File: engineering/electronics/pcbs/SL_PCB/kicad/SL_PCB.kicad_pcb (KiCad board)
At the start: 2 copper layers, 200 x 115 mm, 310 parts, among them J1 - Power +, J17 Temp, J19 Charger +, J32 Temp, J35 ET60S-D06-0-00-D06-X-V1-S, J37 DEBUG, J38 USB, Q1 IRFL4105PBF, Q11 DMG2305UX-7, Q12 DMG2305UX-7, Q13 DMG2305UX-7, Q14 DMG2305UX-7, Q15 DMG2305UX-7, Q16 DMG2305UX-7, Q17 DMG2305UX-7, Q18 DMG2305UX-7, Q19 DMG2305UX-7, Q20 DMG2305UX-7, Q21 DMG2305UX-7, Q22 DMG2305UX-7, Q23 DMG2305UX-7, Q24 DMG2305UX-7, Q25 DMG2305UX-7, Q26 DMG2305UX-7, Q27 DMG2305UX-7, Q28 DMG2305UX-7, Q29 DMG2305UX-7, Q3 IRFL4105PBF, Q30 DMG2305UX-7, Q31 DMG2305UX-7, Q32 DMG2305UX-7, Q33 DMG2305UX-7, Q34 DMG2305UX-7, Q4 IRFL4105PBF

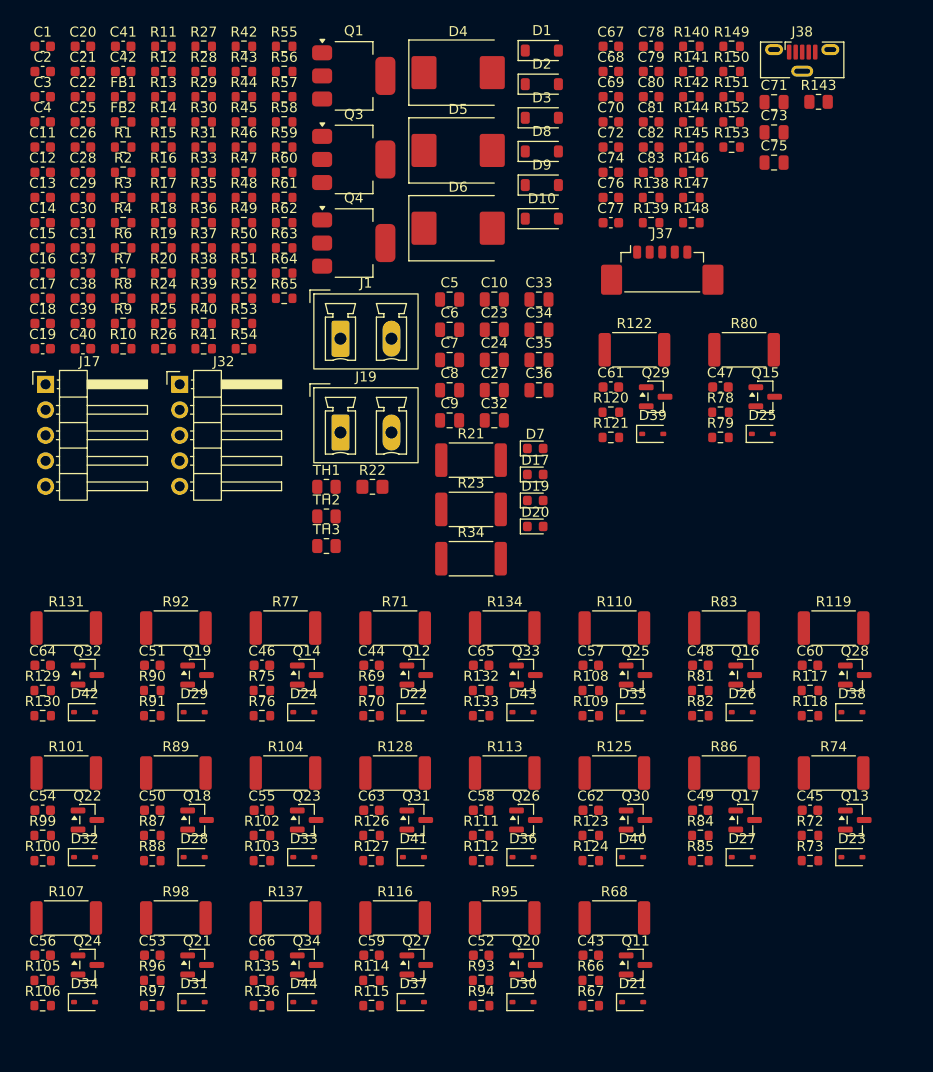
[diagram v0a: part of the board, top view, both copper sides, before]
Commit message: Only leave basic layout in KiCad file
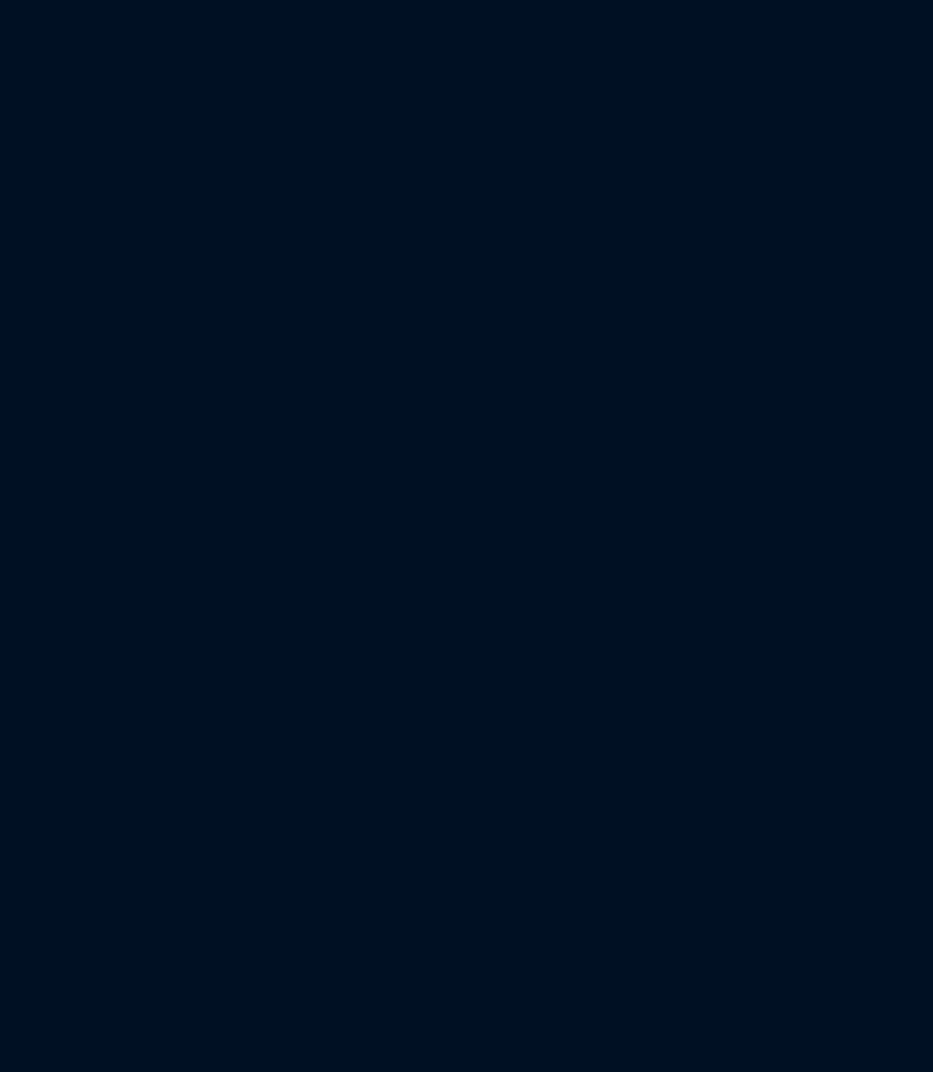
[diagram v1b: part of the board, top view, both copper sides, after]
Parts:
- removed C1, C2, C21, C22: 100p, Capacitor_SMD:C_0603_1608Metric
- removed C10, C27, C32, C33, C34, C35, C36, C5, C6, C7, C71, C73, C8, C9: 1u, Capacitor_SMD:C_0805_2012Metric
- removed C11, C12, C13, C14, C15, C16, C17, C18, C19, C20, C25, C26, C3, C38, C39, C4, C40, C41, C42, C43, C44, C45, C46, C47, C48, C49, C50, C51, C52, C53, C54, C55, C56, C57, C58, C59, C60, C61, C62, C63, C64, C65, C66, C70, C72, C74, C76, C79, C80: 100n, Capacitor_SMD:C_0603_1608Metric
- removed C23, C24: 22u, Capacitor_SMD:C_0805_2012Metric
- removed C28: 47n, Capacitor_SMD:C_0603_1608Metric
- removed C29, C30, C31: 10u, Capacitor_SMD:C_0603_1608Metric
- removed C37, C81, C82, C83: 2.2u, Capacitor_SMD:C_0603_1608Metric
- removed C67, C68: 10n, Capacitor_SMD:C_0603_1608Metric
- removed C69: 1u, Capacitor_SMD:C_0603_1608Metric
- removed C75: 10n, Capacitor_SMD:C_0805_2012Metric
- removed C77, C78: 18p, Capacitor_SMD:C_0603_1608Metric
- removed D1, D2, D8, D9: 1N4148W, Diode_SMD:D_SOD-123
- removed D10, D3: BZT52H-C62, Diode_SMD:D_SOD-123
- removed D17, D7: LED, LED_SMD:LED_0603_1608Metric
- removed D19: POWER, LED_SMD:LED_0603_1608Metric
- removed D20: STATUS, LED_SMD:LED_0603_1608Metric
- removed D21, D22, D23, D24, D25, D26, D27, D28, D29, D30, D31, D32, D33, D34, D35, D36, D37, D38, D39, D40, D41, D42, D43, D44: PDZ7.5B, Diode_SMD:D_SOD-323
- removed D4, D5, D6: smcj150a, Diode_SMD:D_SMC
- removed FB1, FB2: 33, Resistor_SMD:R_0603_1608Metric
- removed J1: - Power +, Connector_Phoenix_MC_HighVoltage:PhoenixContact_MCV_1,5_2-G-5.08_1x02_P5.08mm_Vertical
- removed J17, J32: Temp, Connector_PinHeader_2.54mm:PinHeader_1x05_P2.54mm_Horizontal
- removed J19: Charger +, Connector_Phoenix_MC_HighVoltage:PhoenixContact_MCV_1,5_2-G-5.08_1x02_P5.08mm_Vertical
- removed J37: DEBUG, Connector_Molex:Molex_PicoBlade_53398-0571_1x05-1MP_P1.25mm_Vertical
- removed J38: USB, Connector_USB:USB_Micro-B_Molex-105133-0001
- removed Q1, Q3, Q4: IRFL4105PBF, Package_TO_SOT_SMD:SOT-223
- removed Q11, Q12, Q13, Q14, Q15, Q16, Q17, Q18, Q19, Q20, Q21, Q22, Q23, Q24, Q25, Q26, Q27, Q28, Q29, Q30, Q31, Q32, Q33, Q34: DMG2305UX-7, Package_TO_SOT_SMD:SOT-23
- removed R1, R102, R105, R108, R111, R114, R117, R120, R123, R126, R129, R132, R135, R2, R3, R30, R33, R35, R36, R37, R38, R39, R4, R57, R66, R69, R72, R75, R78, R81, R84, R87, R90, R93, R96, R99: 100, Resistor_SMD:R_0603_1608Metric
- removed R10, R12, R48, R50: 0, Resistor_SMD:R_0603_1608Metric
- removed R100, R103, R106, R109, R112, R115, R118, R121, R124, R127, R130, R133, R136, R141, R31, R46, R6, R60, R67, R70, R73, R76, R79, R82, R85, R88, R91, R94, R97: 1.2k, Resistor_SMD:R_0603_1608Metric
- removed R101, R104, R107, R110, R113, R116, R119, R122, R125, R128, R131, R134, R137, R68, R71, R74, R77, R80, R83, R86, R89, R92, R95, R98: 3.9, Resistor_SMD:R_2512_6332Metric
- removed R11, R49, R58: 1M, Resistor_SMD:R_0603_1608Metric
- removed R13, R19, R8: 10, Resistor_SMD:R_0603_1608Metric
- removed R138, R139: 51, Resistor_SMD:R_0603_1608Metric
- removed R14, R20, R41, R42, R9: 4.7M, Resistor_SMD:R_0603_1608Metric
- removed R140, R47, R7: 806, Resistor_SMD:R_0603_1608Metric
- removed R142, R145: 2.2k, Resistor_SMD:R_0603_1608Metric
- removed R143: 4.7M, Resistor_SMD:R_0805_2012Metric
- removed R144, R15, R16, R17, R18, R25, R26, R51, R52, R53, R54, R59: 100k, Resistor_SMD:R_0603_1608Metric
- removed R146, R147, R152, R29, R55, R56, R61: 10k, Resistor_SMD:R_0603_1608Metric
- removed R148, R149, R153, R24, R27, R28: 4.75k, Resistor_SMD:R_0603_1608Metric
- removed R150, R151: 240, Resistor_SMD:R_0603_1608Metric
- removed R21, R23: 220k, Resistor_SMD:R_2512_6332Metric
- removed R22: 2K2, Resistor_SMD:R_0805_2012Metric_Pad1.20x1.40mm_HandSolder
- removed R34: 100k, Resistor_SMD:R_2512_6332Metric
- removed R40, R43, R44: 1, Resistor_SMD:R_0603_1608Metric
- removed R45: 130k, Resistor_SMD:R_0603_1608Metric
- removed R62, R63, R64: 470, Resistor_SMD:R_0603_1608Metric
- removed R65: 1.5k, Resistor_SMD:R_0603_1608Metric
- removed TH1, TH3: 100k, Resistor_SMD:R_0805_2012Metric
- removed TH2: Thermistor_NTC 100k, Resistor_SMD:R_0805_2012Metric
